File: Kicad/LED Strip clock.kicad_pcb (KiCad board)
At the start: 2 copper layers, 99.1 x 97.8 mm, 86 parts, among them J1 Conn_01x09_Male, J2 Conn_01x09_Male, J3 Conn_01x09_Male, J4 Conn_01x09_Male, J5 Conn_01x04_Male, J6 Barrel_Jack_Switch, U1 TPIC6B595, U10 5611BH, U11 5611BH, U12 5611BH, U13 MCP23008-xSO, U14 INA219AxD, U2 TPIC6B595, U3 TPIC6B595, U4 TPIC6B595, U5 74HCT244, U6 WeMos_D1_mini, U7 MAX809S, U8 L7805, U9 5611BH

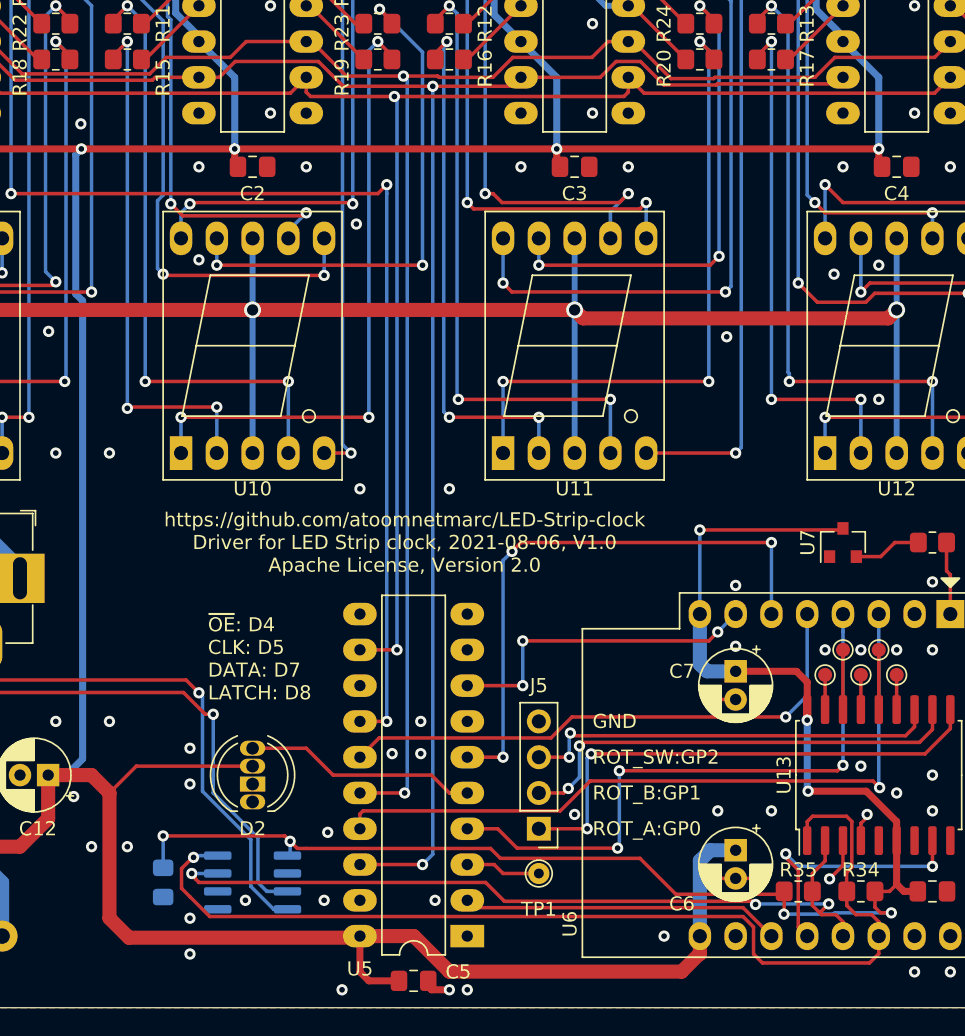
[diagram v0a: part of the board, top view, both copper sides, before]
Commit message: Fixed power-on flash of digits.
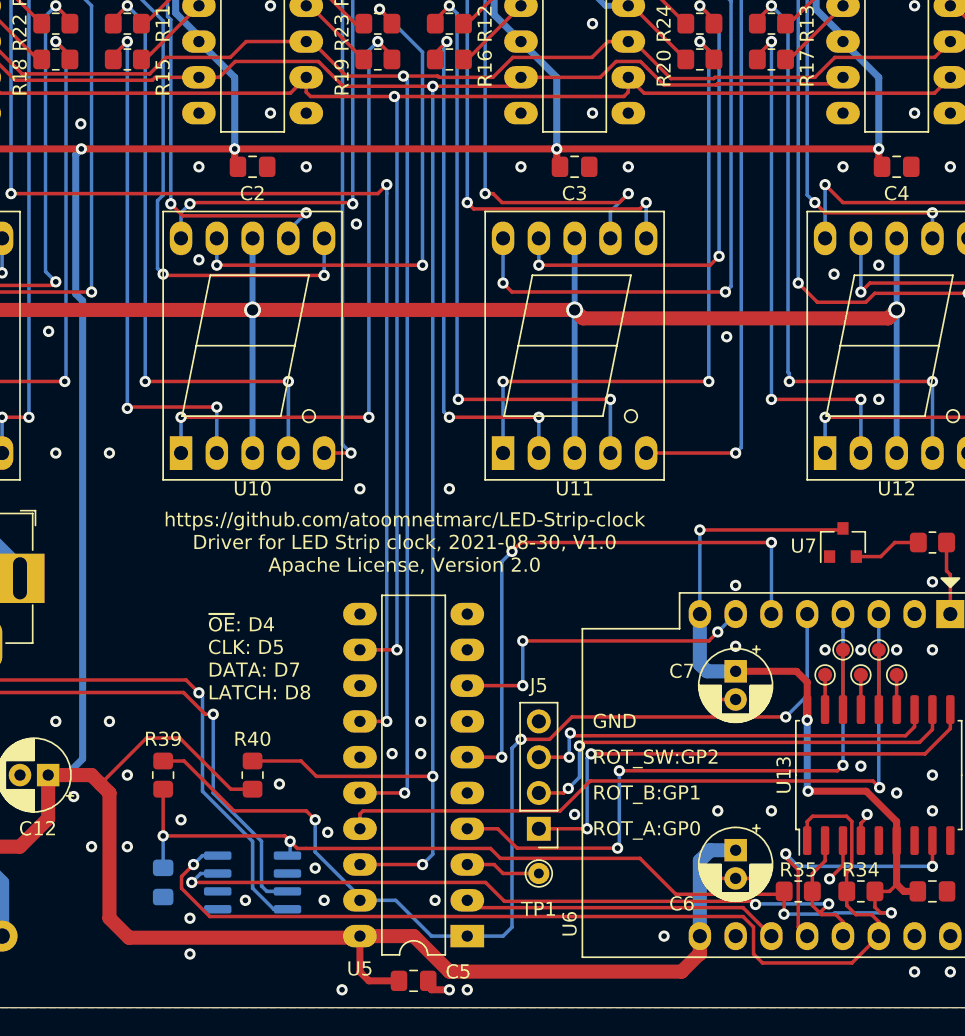
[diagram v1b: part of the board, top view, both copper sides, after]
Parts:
- removed D2: PL9823-F5, LED_THT-extra:LED_D5.0mm-4_PL9823-F5
- added R39: 10K, Resistor_SMD:R_0805_2012Metric_Pad1.20x1.40mm_HandSolder, F.Cu at (174.0, 139.7)
- added R40: 10K, Resistor_SMD:R_0805_2012Metric_Pad1.20x1.40mm_HandSolder, F.Cu at (180.3, 139.7)
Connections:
- U5 pad 1: GND -> /ENBUF
- U5 pad 15: /NEOPIXEL -> GND
- U5 pad 19: GND -> /ENBUF
- U5 pad 5: /NEOPIXEL_5V -> Net-(U5-Pad5)
- U6 pad 5: /NEOPIXEL -> /ENBUF
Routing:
- net /ENBUF: track 0.00 -> 72.6 mm, vias 0 -> 3
- net /NEOPIXEL: track 39.3 -> 0.00 mm, vias 1 -> 0
- net /NEOPIXEL_5V: track 16.6 -> 0.00 mm
- net /~OE_5V: track 132.5 -> 145.8 mm, vias 2 -> 3
- net +3V3: track 111.7 -> 115.1 mm
- net +5V: track 317.0 -> 319.7 mm
- net SCL: track 73.4 -> 72.3 mm
- net GND: vias 107 -> 109
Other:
- board text added: "https://github.com/atoomnetmarc/LED-Strip-clock Driver for LED Strip clock, 2021-08-30, V1.0 Apache License, Version 2.0"
- board text removed: "https://github.com/atoomnetmarc/LED-Strip-clock Driver for LED Strip clock, 2021-08-06, V1.0 Apache License, Version 2.0"

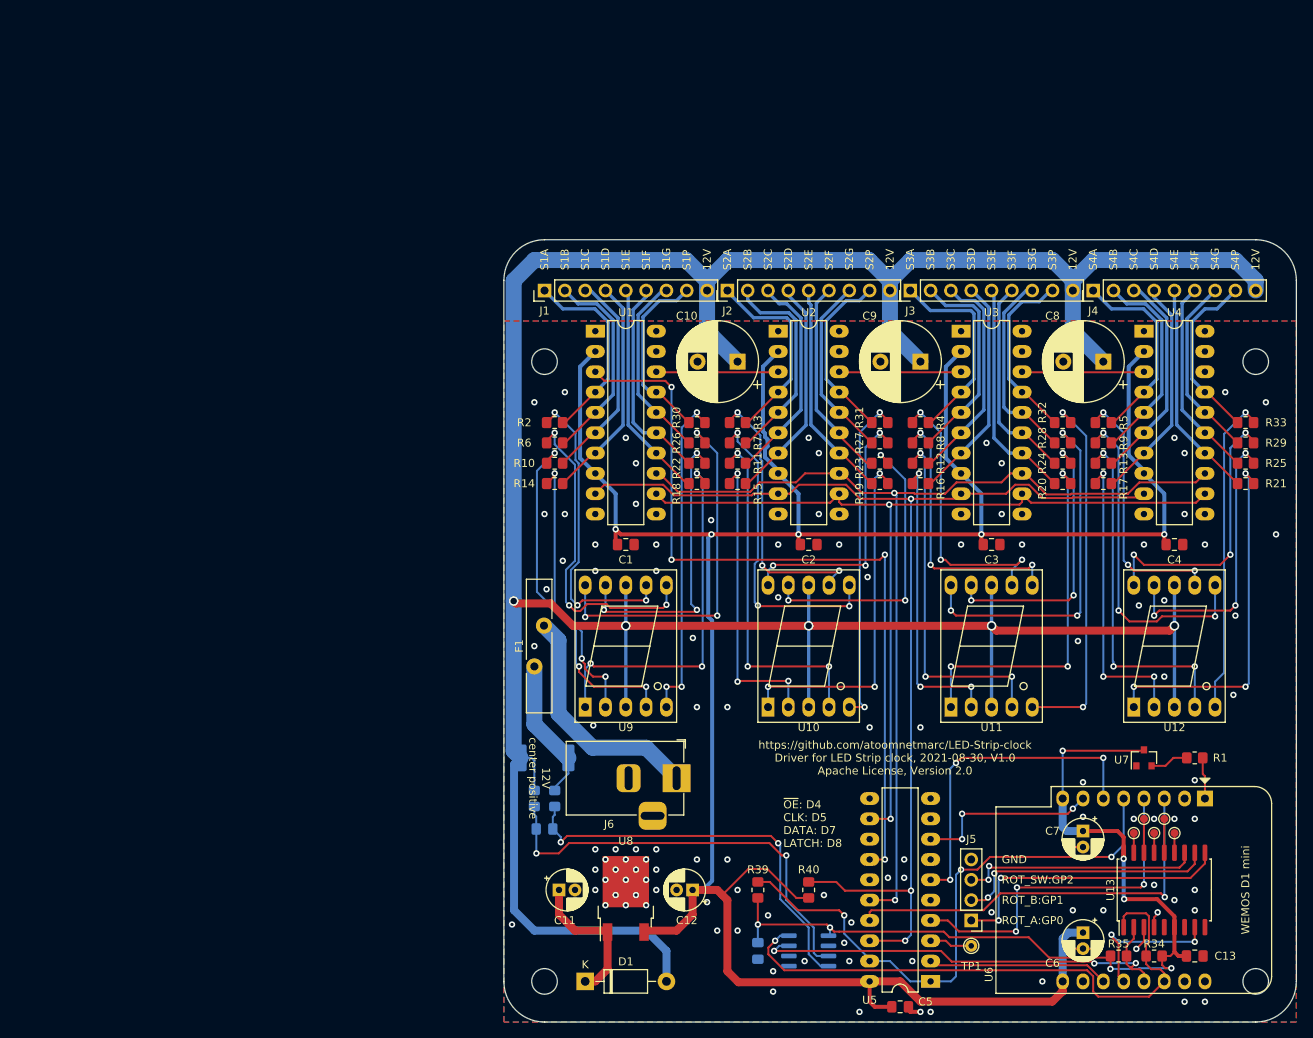
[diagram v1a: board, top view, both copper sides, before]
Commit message: Change board layout. Add RTC. Add seconds LED display.
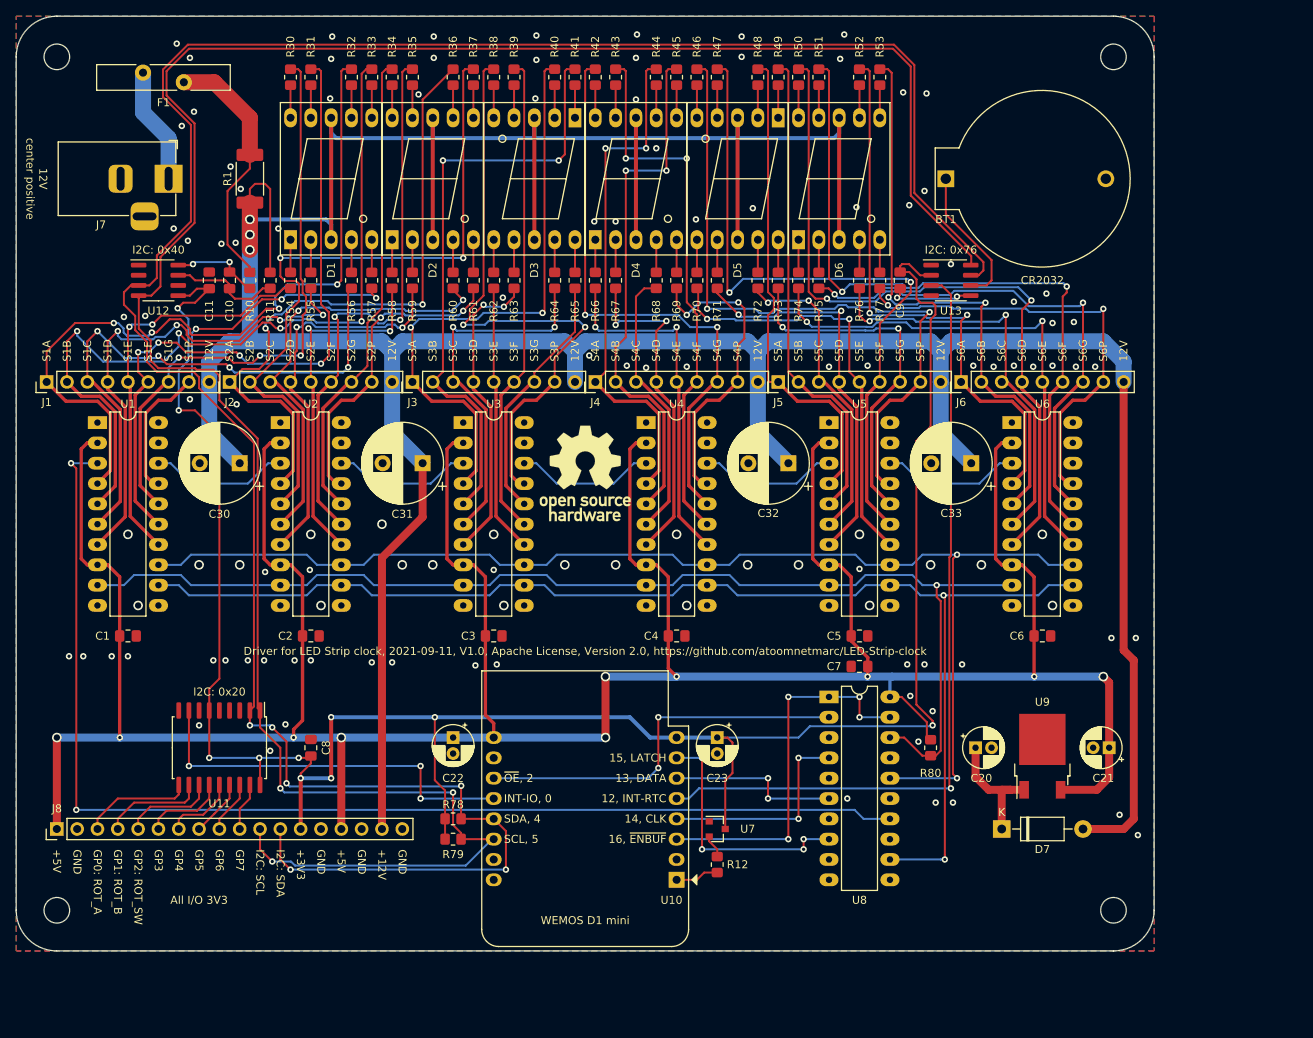
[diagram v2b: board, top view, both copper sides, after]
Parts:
- removed the C10 at (171.4, 73.7)
- removed the R1 at (228.6, 123.2)
- removed the R39 at (174.0, 139.7)
- removed TP1: TestPoint, TestPoint:TestPoint_THTPad_D1.5mm_Drill0.7mm
- removed TP2, TP3, TP4, TP5, TP6: TestPoint, TestPoint:TestPoint_Pad_D1.0mm
- added BT1: CR2032, Battery-extra:BatteryHolder-cr2032, F.Cu at (197.5, 50.8)
- added C32: 2200uF/16v, Capacitor_THT:CP_Radial_D10.0mm_P5.00mm, F.Cu at (177.8, 86.4)
- added C33: 2200uF/16v, Capacitor_THT:CP_Radial_D10.0mm_P5.00mm, F.Cu at (200.7, 86.4)
- added C5: 10uF, Capacitor_SMD:C_0805_2012Metric_Pad1.18x1.45mm_HandSolder, F.Cu at (186.7, 108.0)
- added C6: 10uF, Capacitor_SMD:C_0805_2012Metric_Pad1.18x1.45mm_HandSolder, F.Cu at (209.6, 108.0)
- added C9: 10uF, Capacitor_SMD:C_0805_2012Metric_Pad1.18x1.45mm_HandSolder, F.Cu at (191.8, 63.5)
- added D5: 5611BH, Display_7Segment-extra:5611BH, F.Cu at (171.4, 50.8)
- added D6: 5611BH, Display_7Segment-extra:5611BH, F.Cu at (184.2, 50.8)
- added J5: Conn_01x09_Male, Connector_PinHeader_2.54mm:PinHeader_1x09_P2.54mm_Vertical, F.Cu at (176.5, 76.2)
- added J6: Conn_01x09_Male, Connector_PinHeader_2.54mm:PinHeader_1x09_P2.54mm_Vertical, F.Cu at (199.4, 76.2)
- added R12: 100R, Resistor_SMD:R_0805_2012Metric_Pad1.20x1.40mm_HandSolder, F.Cu at (168.9, 136.5)
- added R46: 4K7, Resistor_SMD:R_0805_2012Metric_Pad1.20x1.40mm_HandSolder, F.Cu at (166.4, 38.1)
- added R47: 4K7, Resistor_SMD:R_0805_2012Metric_Pad1.20x1.40mm_HandSolder, F.Cu at (168.9, 38.1)
- added R48: 4K7, Resistor_SMD:R_0805_2012Metric_Pad1.20x1.40mm_HandSolder, F.Cu at (174.0, 38.1)
- added R49: 4K7, Resistor_SMD:R_0805_2012Metric_Pad1.20x1.40mm_HandSolder, F.Cu at (176.5, 38.1)
- added R50: 4K7, Resistor_SMD:R_0805_2012Metric_Pad1.20x1.40mm_HandSolder, F.Cu at (179.1, 38.1)
- added R51: 4K7, Resistor_SMD:R_0805_2012Metric_Pad1.20x1.40mm_HandSolder, F.Cu at (181.6, 38.1)
- added R52: 4K7, Resistor_SMD:R_0805_2012Metric_Pad1.20x1.40mm_HandSolder, F.Cu at (186.7, 38.1)
- added R53: 4K7, Resistor_SMD:R_0805_2012Metric_Pad1.20x1.40mm_HandSolder, F.Cu at (189.2, 38.1)
- added R70: 4K7, Resistor_SMD:R_0805_2012Metric_Pad1.20x1.40mm_HandSolder, F.Cu at (166.4, 63.5)
- added R71: 4K7, Resistor_SMD:R_0805_2012Metric_Pad1.20x1.40mm_HandSolder, F.Cu at (168.9, 63.5)
- added R72: 4K7, Resistor_SMD:R_0805_2012Metric_Pad1.20x1.40mm_HandSolder, F.Cu at (174.0, 63.5)
- added R73: 4K7, Resistor_SMD:R_0805_2012Metric_Pad1.20x1.40mm_HandSolder, F.Cu at (176.5, 63.5)
- added R74: 4K7, Resistor_SMD:R_0805_2012Metric_Pad1.20x1.40mm_HandSolder, F.Cu at (179.1, 63.5)
- added R75: 4K7, Resistor_SMD:R_0805_2012Metric_Pad1.20x1.40mm_HandSolder, F.Cu at (181.6, 63.5)
- added R76: 4K7, Resistor_SMD:R_0805_2012Metric_Pad1.20x1.40mm_HandSolder, F.Cu at (186.7, 63.5)
- added R77: 4K7, Resistor_SMD:R_0805_2012Metric_Pad1.20x1.40mm_HandSolder, F.Cu at (189.2, 63.5)
- added REF**: OSHW-Logo_11.4x12mm_SilkScreen, Symbol:OSHW-Logo_11.4x12mm_SilkScreen, F.Cu at (152.4, 87.6)
- added U13: DS3231MZ, Package_SO:SOIC-8_3.9x4.9mm_P1.27mm, F.Cu at (198.1, 63.5)
- added U5: TPIC6B595, Package_DIP:DIP-20_W7.62mm_LongPads, F.Cu at (182.9, 81.3)
- added U6: TPIC6B595, Package_DIP:DIP-20_W7.62mm_LongPads, F.Cu at (205.7, 81.3)
- C10: renamed from C15; value 1uF -> 10uF; moved to F.Cu
- C11: renamed from C14; moved to F.Cu
- C21: renamed from C12; value 33uF/16v -> 100uF/16v
- J8: renamed from J5; value Conn_01x04_Male -> Conn_01x18_Male; footprint Connector_PinHeader_2.54mm:PinHeader_1x04_P2.54mm_Vertical -> Connector_PinHeader_2.54mm:PinHeader_1x18_P2.54mm_Vertical
- R1: renamed from R36; moved to F.Cu
- R10: renamed from R37; value 10R -> 100R; moved to F.Cu
- R11: renamed from R38; value 10R -> 100R; moved to F.Cu
- R80: renamed from R40; value 10K -> 4K7
- U12: renamed from U14; moved to F.Cu
- moved U11 119.4 mm to (106.7, 121.9), turned to 270 degrees
- moved U12 116.8 mm to (99.1, 63.5)
- moved J8 114.9 mm to (86.4, 132.1), turned to 90 degrees
- moved C8 113.5 mm to (118.1, 121.9), turned to 90 degrees
- moved C30 108.7 mm to (109.2, 86.4)
- moved C11 108.3 mm to (105.4, 63.5), turned to 90 degrees
- moved J7 98.2 mm to (100.3, 50.8)
- moved R42 93.3 mm to (153.7, 38.1), turned to 90 degrees
- moved R43 92.4 mm to (156.2, 38.1), turned to 90 degrees
- moved D4 89.1 mm to (158.8, 50.8)
- moved R79 88.8 mm to (135.9, 133.3), turned to 180 degrees
- moved F1 85.2 mm to (102.2, 38.7), turned to 180 degrees
- moved R66 85.2 mm to (153.7, 63.5), turned to 270 degrees
- moved R78 84.9 mm to (135.9, 130.8)
- moved R38 83.2 mm to (141.0, 38.1), turned to 90 degrees
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- renumbered C11 to C20, C6 to C22, C7 to C23, C8 to C30, C9 to C31, C5 to C7, C13 to C8, U9 to D1, U10 to D2, U11 to D3, U12 to D4, D1 to D7, J6 to J7, R26 to R30, R22 to R31, R2 to R32, R6 to R33, R27 to R34, R23 to R35, R3 to R36, R7 to R37, R32 to R38, R12 to R39, R16 to R40, R20 to R41, R29 to R42, R25 to R43, R5 to R44, R9 to R45, R18 to R54, R14 to R55, R10 to R56, R30 to R57, R19 to R58, R15 to R59, R11 to R60, R31 to R61, R8 to R62, R4 to R63, R24 to R64, R28 to R65, R21 to R66, R17 to R67, R13 to R68, R33 to R69, R35 to R78, R34 to R79, U6 to U10, U13 to U11, U5 to U8, U8 to U9
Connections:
- net INT renamed INT-IO
- net VIN+ renamed Net-(F1-Pad1)
- J8 pad 1: /ROT_A -> +5V
- J8 pad 2: /ROT_B -> GND
- J8 pad 3: /ROT_SW -> /ROT_A
- J8 pad 4: GND -> /ROT_B
- R39 pad 2: /S3C -> /S3F
- R40 pad 2: /S3D -> /S3A
- R41 pad 2: /S3E -> /S3B
- R62 pad 2: /S3B -> /S3E
- R63 pad 2: /S3A -> /S3D
- R64 pad 2: /S3F -> /S3C
- U10 pad 3: Net-(U5-Pad17) -> /~ENBUF
- U10 pad 5: /ENBUF -> INT-RTC
- U11 pad 13: Net-(TP2-Pad1) -> /GP3
- U11 pad 14: Net-(TP3-Pad1) -> /GP4
- U11 pad 15: Net-(TP4-Pad1) -> /GP5
- U11 pad 16: Net-(TP5-Pad1) -> /GP6
- U11 pad 17: Net-(TP6-Pad1) -> /GP7
- U8 pad 1: /ENBUF -> /~ENBUF
- U8 pad 17: Net-(U5-Pad17) -> GND
- U8 pad 19: /ENBUF -> /~ENBUF
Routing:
- net SDA: track 57.6 -> 305.6 mm, vias 3 -> 6
- net SCL: track 72.3 -> 295.4 mm, vias 1 -> 3
- net +3V3: track 115.1 -> 280.7 mm, vias 7 -> 10
- net +12V: track 394.1 -> 515.8 mm, vias 5 -> 3
- net +5V: track 319.7 -> 423.6 mm, vias 5 -> 10
- net INT-RTC: track 0.00 -> 99.6 mm, vias 0 -> 1
- net /S6G: track 0.00 -> 93.4 mm, vias 0 -> 2
- net /S6F: track 0.00 -> 90.5 mm, vias 0 -> 2
- net /S5F: track 0.00 -> 86.4 mm, vias 0 -> 2
- net /S5DP: track 0.00 -> 86.0 mm, vias 0 -> 2
- net /S1B: track 25.7 -> 102.0 mm, vias 0 -> 4
- net /ENBUF: track 72.6 -> 0.00 mm, vias 3 -> 0
- net /S6B: track 0.00 -> 72.6 mm, vias 0 -> 2
- net /S6A: track 0.00 -> 71.9 mm, vias 0 -> 2
- net /S1A: track 24.7 -> 96.0 mm, vias 0 -> 4
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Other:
- board size 99.1 x 97.8 mm -> 142.2 x 116.8 mm
- board text added: "+12V"
- board text added: "+3V3"
- board text added: "+5V"
- board text added: "12, INT-RTC"
- board text added: "13, DATA"
- board text added: "14, CLK"
- board text added: "15, LATCH"
- board text added: "16, ~ENBUF~"
- board text added: "All I/O 3V3"
- board text added: "CR2032"
- board text added: "Driver for LED Strip clock, 2021-09-11, V1.0, Apache License, Version 2.0, https://github.com/atoomnetmarc/LED-Strip-clock"
- board text added: "GP0: ROT_A"
- board text added: "GP1: ROT_B"
- board text added: "GP2: ROT_SW"
- board text added: "GP3"
- board text added: "GP4"
- board text added: "GP5"
- board text added: "GP6"
- board text added: "GP7"
- board text added: "I2C: 0x20"
- board text added: "I2C: 0x40"
- board text added: "I2C: 0x76"
- board text added: "I2C: SCL"
- board text added: "I2C: SDA"
- board text added: "INT-IO, 0"
- board text added: "S5A"
- board text added: "S5B"
- board text added: "S5C"
- board text added: "S5D"
- board text added: "S5E"
- board text added: "S5F"
- board text added: "S5G"
- board text added: "S5P"
- board text added: "S6A"
- board text added: "S6B"
- board text added: "S6C"
- board text added: "S6D"
- board text added: "S6E"
- board text added: "S6F"
- board text added: "S6G"
- board text added: "S6P"
- board text added: "SCL, 5"
- board text added: "SDA, 4"
- board text added: "~OE~, 2"
- board text removed: "ROT_A:GP0"
- board text removed: "ROT_B:GP1"
- board text removed: "ROT_SW:GP2"
- board text removed: "https://github.com/atoomnetmarc/LED-Strip-clock Driver for LED Strip clock, 2021-08-30, V1.0 Apache License, Version 2.0"
- board text removed: "~OE~: D4 CLK: D5 DATA: D7 LATCH: D8"
